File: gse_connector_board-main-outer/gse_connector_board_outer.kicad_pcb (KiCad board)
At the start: 2 copper layers, 52.2 x 27 mm, 9 parts, among them J1 arming_connector, J2 gse_com_connector, J3 chg_connector, J5 Conn_02x02_Top_Bottom, J6 Conn_02x02_Top_Bottom, J7 Conn_02x02_Top_Bottom

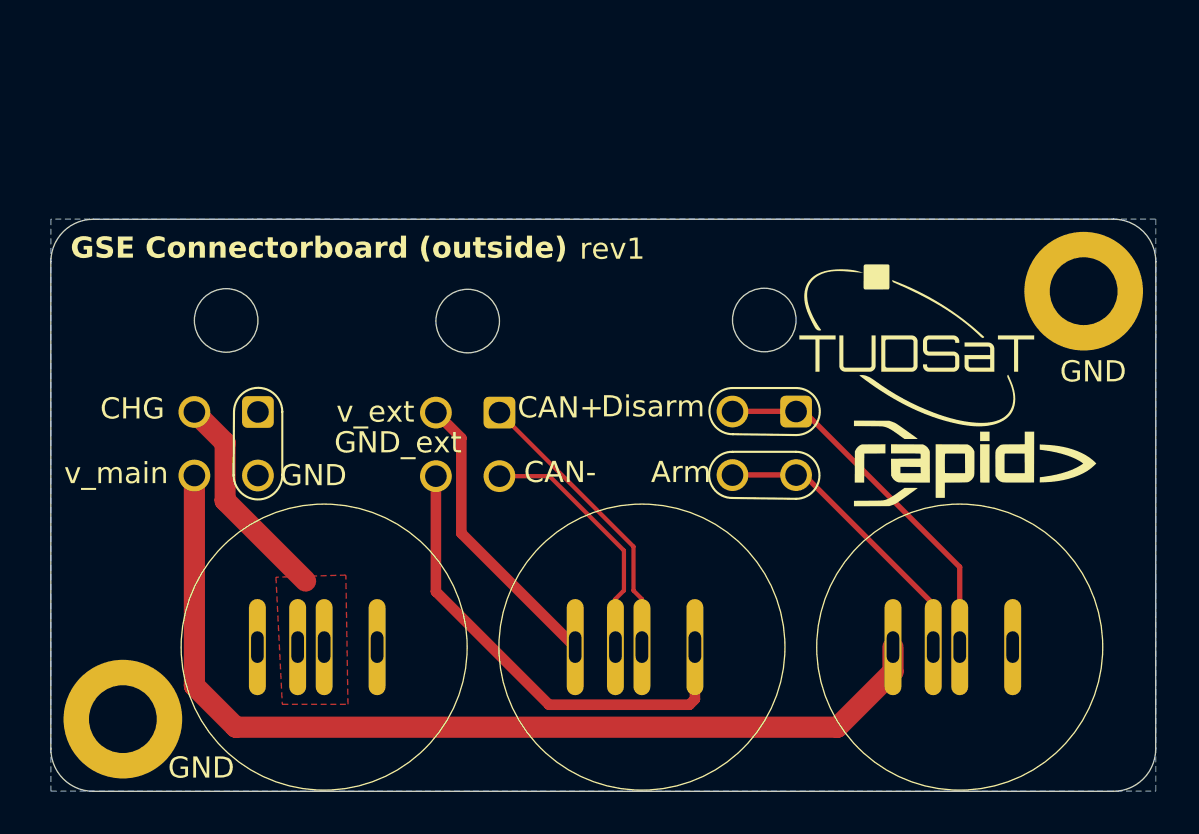
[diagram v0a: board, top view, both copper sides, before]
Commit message: fix silkscreen
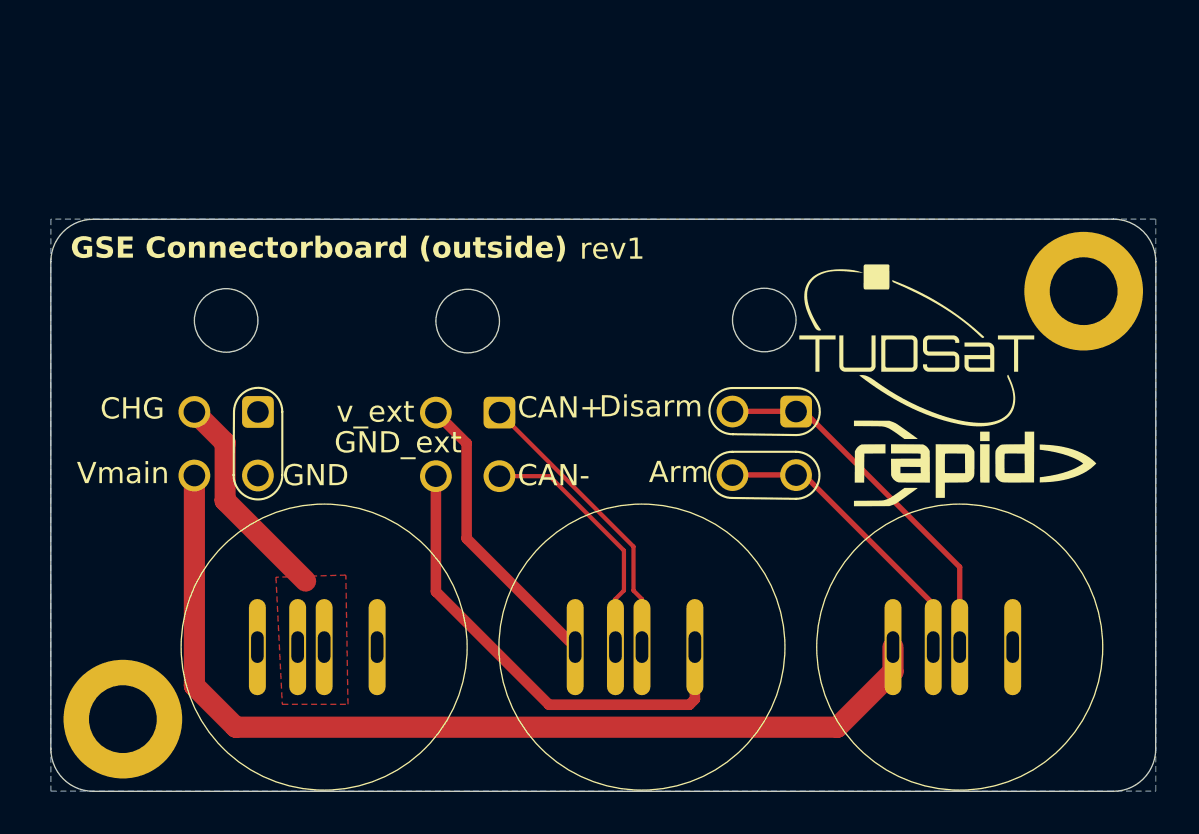
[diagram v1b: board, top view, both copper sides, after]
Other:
- board text added: "Vmain"
- board text removed: "v_main"
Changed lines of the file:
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@@
 			(at 7.975 7.47 0)
 			(layer "B.SilkS")
+			(hide yes)
 			(effects
 				(font
@@
 			(at 1.5 10.12 0)
 			(layer "B.SilkS")
+			(hide yes)
 			(effects
 				(font
@@
 			(at 1.5 10.12 0)
 			(layer "B.SilkS")
+			(hide yes)
 			(effects
 				(font
@@
 		(layer "Edge.Cuts")
 	)
-	(gr_text "v_main\n"
-		(at 111 93.9 0)
+	(gr_text "Vmain\n"
+		(at 111.6 93.9 0)
 		(layer "F.SilkS")
 		(effects
@@
 	)
 	(gr_text "GND"
-		(at 115.9 107.8 0)
-		(layer "F.SilkS")
-		(effects
-			(font
-				(size 1 1)
-				(thickness 0.15)
-			)
-			(justify left bottom)
-		)
-	)
-	(gr_text "GND"
-		(at 121.2 94 0)
+		(at 121.3 94 0)
 		(layer "F.SilkS")
 		(effects
@@
 	)
 	(gr_text "CAN-"
-		(at 132.7 93.85 0)
+		(at 132.4 94 0)
 		(layer "F.SilkS")
 		(effects
@@
 	)
 	(gr_text "Disarm\n"
-		(at 136.35 90.75 0)
+		(at 136.25 90.75 0)
 		(layer "F.SilkS")
 		(effects
@@
 	)
 	(gr_text "Arm"
-		(at 138.7 93.85 0)
-		(layer "F.SilkS")
-		(effects
-			(font
-				(size 1 1)
-				(thickness 0.15)
-			)
-			(justify left bottom)
-		)
-	)
-	(gr_text "GND"
-		(at 158 89.1 0)
+		(at 138.6 93.85 0)
 		(layer "F.SilkS")
 		(effects
@@
 		)
 	)
-	(gr_text "v_main\n"
-		(at 150.62 93.79 90)
+	(gr_text "Vmain\n"
+		(at 150.62 94.39 90)
 		(layer "B.SilkS")
 		(effects
@@
 	)
 	(segment
-		(start 128.55 90.45)
-		(end 129.75 91.65)
-		(width 0.5)
-		(layer "F.Cu")
-		(net "+V_EXT")
-	)
-	(segment
-		(start 129.75 96.144238)
+		(start 130 96.394238)
 		(end 135.124744 101.518982)
 		(width 0.5)
@@
 	)
 	(segment
-		(start 129.75 91.65)
-		(end 129.75 96.144238)
+		(start 128.55 90.45)
+		(end 130 91.9)
+		(width 0.5)
+		(layer "F.Cu")
+		(net "+V_EXT")
+	)
+	(segment
+		(start 130 91.9)
+		(end 130 96.394238)
 		(width 0.5)
 		(layer "F.Cu")
@@
 		(hatch edge 0.5)
 		(priority 1)
-		(connect_pads
+		(connect_pads yes
 			(clearance 0)
 		)

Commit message: edited grounding and edge cuts
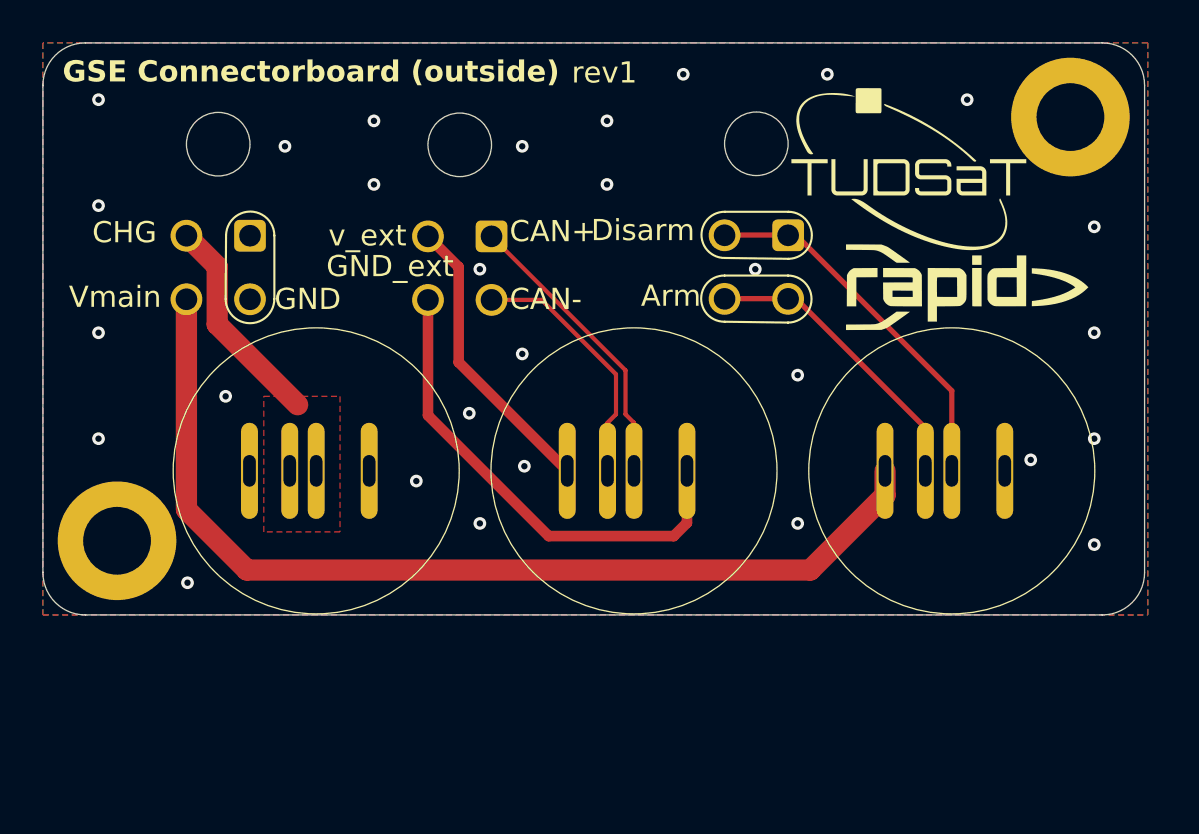
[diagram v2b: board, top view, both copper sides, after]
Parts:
- moved H1 8.42 mm to (113.5, 96.5)
- moved J5 8.33 mm to (145.2, 82.1)
- moved J6 8.33 mm to (131.2, 82.1)
- moved J7 8.33 mm to (119.8, 82.1)
- moved G*** 8.33 mm to (153.6, 84.5)
- moved J1 8.33 mm to (152.9, 96.2)
- moved J2 8.33 mm to (137.9, 96.2)
- moved J3 8.33 mm to (122.9, 96.2)
- moved H2 8.24 mm to (158.5, 76.5)
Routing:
- net main_voltage: track 46.0 -> 46.7 mm
- net GND: vias 0 -> 29
- added copper zone on F.Cu, net GND
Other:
- board size 52.2 x 27 mm -> 52 x 27 mm
